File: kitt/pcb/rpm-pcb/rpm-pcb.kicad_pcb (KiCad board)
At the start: 2 copper layers, 0 parts

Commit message: placed rpm leds
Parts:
- added C1: 100nF, Capacitor_THT:C_Rect_L7.0mm_W3.5mm_P5.00mm, F.Cu at (287.7, -26.9)
- added C10: 100nF, Capacitor_THT:C_Rect_L7.0mm_W3.5mm_P5.00mm, F.Cu at (213.9, 50.4)
- added C11: 100nF, Capacitor_THT:C_Rect_L7.0mm_W3.5mm_P5.00mm, F.Cu at (128.4, 45.3)
- added C12: 100nF, Capacitor_THT:C_Rect_L7.0mm_W3.5mm_P5.00mm, F.Cu at (181.5, 48.3)
- added C13: 100nF, Capacitor_THT:C_Rect_L7.0mm_W3.5mm_P5.00mm, F.Cu at (128.4, 50.3)
- added C2: 1uF, Capacitor_THT:C_Rect_L7.0mm_W3.5mm_P5.00mm, F.Cu at (296.2, -31.9)
- added C3: 100nF, Capacitor_THT:C_Rect_L7.0mm_W3.5mm_P5.00mm, F.Cu at (287.7, -31.9)
- added C4: 100nF, Capacitor_THT:C_Rect_L7.0mm_W3.5mm_P5.00mm, F.Cu at (305.8, -42.7)
- added C5: 100nF, Capacitor_THT:C_Rect_L7.0mm_W3.5mm_P5.00mm, F.Cu at (305.8, -47.7)
- added C6: 100nF, Capacitor_THT:C_Rect_L7.0mm_W3.5mm_P5.00mm, F.Cu at (250.7, 14.5)
- added C7: 100nF, Capacitor_THT:C_Rect_L7.0mm_W3.5mm_P5.00mm, F.Cu at (250.7, 9.45)
- added C8: 100nF, Capacitor_THT:C_Rect_L7.0mm_W3.5mm_P5.00mm, F.Cu at (231.0, 33.7)
- added C9: 1uF, Capacitor_THT:C_Rect_L7.0mm_W3.5mm_P5.00mm, F.Cu at (243.2, 21.6)
- added CG1: LED, KITT-Footpads:Flangeless_LED, F.Cu at (67.2, 116.8)
- added CG10: LED, KITT-Footpads:Flangeless_LED, F.Cu at (107.1, 93.7)
- added CG11: LED, KITT-Footpads:Flangeless_LED, F.Cu at (112.0, 92.0)
- added CG12: LED, KITT-Footpads:Flangeless_LED, F.Cu at (116.9, 90.6)
- added CG13: LED, KITT-Footpads:Flangeless_LED, F.Cu at (121.9, 89.4)
- added CG14: LED, KITT-Footpads:Flangeless_LED, F.Cu at (126.9, 88.3)
- added CG15: LED, KITT-Footpads:Flangeless_LED, F.Cu at (132.0, 87.5)
- added CG16: LED, KITT-Footpads:Flangeless_LED, F.Cu at (137.1, 86.9)
- added CG17: LED, KITT-Footpads:Flangeless_LED, F.Cu at (142.2, 86.5)
- added CG18: LED, KITT-Footpads:Flangeless_LED, F.Cu at (147.4, 86.2)
- added CG19: LED, KITT-Footpads:Flangeless_LED, F.Cu at (152.5, 86.2)
- added CG2: LED, KITT-Footpads:Flangeless_LED, F.Cu at (71.2, 113.5)
- added CG20: LED, KITT-Footpads:Flangeless_LED, F.Cu at (157.7, 86.5)
- added CG21: LED, KITT-Footpads:Flangeless_LED, F.Cu at (162.8, 86.9)
- added CG22: LED, KITT-Footpads:Flangeless_LED, F.Cu at (167.9, 87.5)
- added CG23: LED, KITT-Footpads:Flangeless_LED, F.Cu at (173.0, 88.3)
- added CG24: LED, KITT-Footpads:Flangeless_LED, F.Cu at (178.1, 89.4)
- added CG25: LED, KITT-Footpads:Flangeless_LED, F.Cu at (183.1, 90.7)
- added CG26: LED, KITT-Footpads:Flangeless_LED, F.Cu at (188.0, 92.0)
- added CG27: LED, KITT-Footpads:Flangeless_LED, F.Cu at (258.5, 19.9)
- added CG28: LED, KITT-Footpads:Flangeless_LED, F.Cu at (192.9, 93.7)
- added CG29: LED, KITT-Footpads:Flangeless_LED, F.Cu at (197.7, 95.5)
- added CG3: LED, KITT-Footpads:Flangeless_LED, F.Cu at (75.3, 110.4)
- added CG30: LED, KITT-Footpads:Flangeless_LED, F.Cu at (202.5, 97.5)
- added CG4: LED, KITT-Footpads:Flangeless_LED, F.Cu at (79.5, 107.5)
- added CG5: LED, KITT-Footpads:Flangeless_LED, F.Cu at (83.9, 104.8)
- added CG6: LED, KITT-Footpads:Flangeless_LED, F.Cu at (88.3, 102.2)
- added CG7: LED, KITT-Footpads:Flangeless_LED, F.Cu at (92.9, 99.8)
- added CG8: LED, KITT-Footpads:Flangeless_LED, F.Cu at (97.5, 97.5)
- added CG9: LED, KITT-Footpads:Flangeless_LED, F.Cu at (102.3, 95.5)
- added CT_DISP1: LDS-A816RI, KITT-Footpads:LDS-A816RI, F.Cu at (132.2, 104.6)
- added CT_DISP2: LDS-A816RI, KITT-Footpads:LDS-A816RI, F.Cu at (152.5, 104.6)
- added J1: Screw_Terminal_01x02, KITT-Footpads:5mm_Screw_Terminal_01x02, F.Cu at (316.1, -54.4)
- added J2: Screw_Terminal_01x02, KITT-Footpads:5mm_Screw_Terminal_01x02, F.Cu at (182.7, 41.0)
- added KEG_1_CAP_L1: 125807R, KITT-Footpads:LED_12_Segment_2.0mm_24_pin, F.Cu at (125.5, -9.80)
- added KEG_1_CAP_R1: 125807R, KITT-Footpads:LED_12_Segment_2.0mm_24_pin, F.Cu at (117.4, -68.9)
- added KEG_1_T1: STBD01-4R8GA, KITT-Footpads:LED_12_Segment_2.0mm_24_pin, F.Cu at (223.0, -68.9)
- added KEG_2_T1: STBD01-4R8GA, KITT-Footpads:LED_12_Segment_2.0mm_24_pin, F.Cu at (214.9, -68.9)
- added KEG_3_T1: STBD01-4R8GA, KITT-Footpads:LED_12_Segment_2.0mm_24_pin, F.Cu at (206.7, -68.9)
- added KEG_4_T1: STBD01-4R8GA, KITT-Footpads:LED_12_Segment_2.0mm_24_pin, F.Cu at (198.6, -68.9)
- added KEG_5_T1: STBD01-4R8GA, KITT-Footpads:LED_12_Segment_2.0mm_24_pin, F.Cu at (190.5, -68.9)
- added KEG_CAP_2_L1: 125807R, KITT-Footpads:LED_12_Segment_2.0mm_24_pin, F.Cu at (182.4, -68.9)
- added KEG_CAP_2_R1: 125807R, KITT-Footpads:LED_12_Segment_2.0mm_24_pin, F.Cu at (174.3, -68.9)
- added KEG_CAP_3_L1: 125807R, KITT-Footpads:LED_12_Segment_2.0mm_24_pin, F.Cu at (166.1, -68.9)
- added KEG_CAP_3_R1: 125807R, KITT-Footpads:LED_12_Segment_2.0mm_24_pin, F.Cu at (158.0, -68.9)
- added LAGER_1_T_L1: 125807R, KITT-Footpads:LED_12_Segment_2.0mm_24_pin, F.Cu at (149.9, -68.9)
- added LAGER_1_T_R1: STBD01-4R8GA, KITT-Footpads:LED_12_Segment_2.0mm_24_pin, F.Cu at (141.8, -68.9)
- added LAGER_2_T_L1: 125807R, KITT-Footpads:LED_12_Segment_2.0mm_24_pin, F.Cu at (133.7, -68.9)
- added LAGER_2_T_R1: STBD01-4R8GA, KITT-Footpads:LED_12_Segment_2.0mm_24_pin, F.Cu at (125.5, -68.9)
- added LAGER_3_T_L1: 125807R, KITT-Footpads:LED_12_Segment_2.0mm_24_pin, F.Cu at (117.4, -9.80)
- added LAGER_3_T_R1: STBD01-4R8GA, KITT-Footpads:LED_12_Segment_2.0mm_24_pin, F.Cu at (133.7, -9.80)
- added LINE_T1: STBD01-4R8GA, KITT-Footpads:LED_12_Segment_2.0mm_24_pin, F.Cu at (231.1, -68.9)
- added LVL1: LVL_5V_3V3, KITT-Footpads:LVL_5V_3V3, F.Cu at (227.0, 23.0)
- added LVL2: LVL_5V_3V3, KITT-Footpads:LVL_5V_3V3, F.Cu at (283.7, -36.1)
- added LVL3: LVL_5V_3V3, KITT-Footpads:LVL_5V_3V3, F.Cu at (314.7, -73.3)
- added MH1: MountingHole, MountingHole:MountingHole_3.2mm_M3, F.Cu at (62.0, 71.5)
- added MH2: MountingHole, MountingHole:MountingHole_3.2mm_M3, F.Cu at (202.0, 71.5)
- added MH3: MountingHole, MountingHole:MountingHole_3.2mm_M3, F.Cu at (248.0, 71.5)
- added MH4: MountingHole, MountingHole:MountingHole_3.2mm_M3, F.Cu at (344.0, 71.5)
- added MH5: MountingHole, MountingHole:MountingHole_3.2mm_M3, F.Cu at (62.0, 195.5)
- added MH6: MountingHole, MountingHole:MountingHole_3.2mm_M3, F.Cu at (202.0, 195.5)
- added MH7: MountingHole, MountingHole:MountingHole_3.2mm_M3, F.Cu at (248.0, 195.5)
- added MH8: MountingHole, MountingHole:MountingHole_3.2mm_M3, F.Cu at (344.0, 195.5)
- added NT1: Net-Tie_3_Tee, NetTie:NetTie-3_THT_Pad0.3mm, F.Cu at (119.0, 51.9)
- added NT10: Net-Tie_3_Tee, NetTie:NetTie-3_THT_Pad0.3mm, F.Cu at (194.8, 50.8)
- added NT11: Net-Tie_3_Tee, NetTie:NetTie-3_THT_Pad0.3mm, F.Cu at (287.0, -37.4)
- added NT12: Net-Tie_3_Tee, NetTie:NetTie-3_THT_Pad0.3mm, F.Cu at (199.3, 50.8)
- added NT13: Net-Tie_3_Tee, NetTie:NetTie-3_THT_Pad0.3mm, F.Cu at (114.4, 51.9)
- added NT2: Net-Tie_3_Tee, NetTie:NetTie-3_THT_Pad0.3mm, F.Cu at (224.6, -3.36)
- added NT3: Net-Tie_3_Tee, NetTie:NetTie-3_THT_Pad0.3mm, F.Cu at (167.5, 50.3)
- added NT4: Net-Tie_3_Tee, NetTie:NetTie-3_THT_Pad0.3mm, F.Cu at (172.0, 50.3)
- added NT5: Net-Tie_3_Tee, NetTie:NetTie-3_THT_Pad0.3mm, F.Cu at (229.1, -3.36)
- added NT6: Net-Tie_3_Tee, NetTie:NetTie-3_THT_Pad0.3mm, F.Cu at (176.6, 51.9)
- added NT7: Net-Tie_3_Tee, NetTie:NetTie-3_THT_Pad0.3mm, F.Cu at (181.1, 51.9)
- added NT8: Net-Tie_3_Tee, NetTie:NetTie-3_THT_Pad0.3mm, F.Cu at (185.7, 51.9)
- added NT9: Net-Tie_3_Tee, NetTie:NetTie-3_THT_Pad0.3mm, F.Cu at (190.2, 50.8)
- added PEG1: MountingHole, MountingHole:MountingHole_5.3mm_M5, F.Cu at (45.0, 72.0)
- added PEG2: MountingHole, MountingHole:MountingHole_5.3mm_M5, F.Cu at (220.0, 72.0)
- added PEG3: MountingHole, MountingHole:MountingHole_5.3mm_M5, F.Cu at (445.0, 72.0)
- added PEG4: MountingHole, MountingHole:MountingHole_5.3mm_M5, F.Cu at (45.0, 197.0)
- added PEG5: MountingHole, MountingHole:MountingHole_5.3mm_M5, F.Cu at (220.0, 197.0)
- added PEG6: MountingHole, MountingHole:MountingHole_5.3mm_M5, F.Cu at (445.0, 197.0)
- added PWR1: OKI-78SR-5_1.5-W36H-C, Converter_DCDC:Converter_DCDC_muRata_OKI-78SR_Horizontal, F.Cu at (260.3, -36.3)
- added Q1: NDP6020P, Package_TO_SOT_THT:TO-220-3_Vertical, F.Cu at (226.7, -6.47)
- added Q2: NDP6020P, Package_TO_SOT_THT:TO-220-3_Vertical, F.Cu at (226.7, -12.4)
- added Q3: NDP6020P, Package_TO_SOT_THT:TO-220-3_Vertical, F.Cu at (320.1, -63.5)
- added Q4: NDP6020P, Package_TO_SOT_THT:TO-220-3_Vertical, F.Cu at (333.4, -71.6)
- added Q5: NDP6020P, Package_TO_SOT_THT:TO-220-3_Vertical, F.Cu at (273.4, -13.2)
- added Q6: NDP6020P, Package_TO_SOT_THT:TO-220-3_Vertical, F.Cu at (215.4, 45.9)
- added R1: 120R, Resistor_THT:R_Axial_DIN0207_L6.3mm_D2.5mm_P10.16mm_Horizontal, F.Cu at (301.3, -52.3)
- added R10: 120R, Resistor_THT:R_Axial_DIN0207_L6.3mm_D2.5mm_P10.16mm_Horizontal, F.Cu at (280.1, -44.6)
- added R11: 120R, Resistor_THT:R_Axial_DIN0207_L6.3mm_D2.5mm_P10.16mm_Horizontal, F.Cu at (168.0, 47.2)
- added R12: 120R, Resistor_THT:R_Axial_DIN0207_L6.3mm_D2.5mm_P10.16mm_Horizontal, F.Cu at (168.0, 43.2)
- added R13: 10K, Resistor_THT:R_Axial_DIN0207_L6.3mm_D2.5mm_P10.16mm_Horizontal, F.Cu at (168.0, 39.1)
- added R14: 2.2K, Resistor_THT:R_Axial_DIN0207_L6.3mm_D2.5mm_P10.16mm_Horizontal, F.Cu at (114.9, 48.8)
- added R15: 2.2K, Resistor_THT:R_Axial_DIN0207_L6.3mm_D2.5mm_P10.16mm_Horizontal, F.Cu at (114.9, 44.8)
- added R16: 2.2K, Resistor_THT:R_Axial_DIN0207_L6.3mm_D2.5mm_P10.16mm_Horizontal, F.Cu at (225.1, 0.85)
- added R17: 2.2K, Resistor_THT:R_Axial_DIN0207_L6.3mm_D2.5mm_P10.16mm_Horizontal, F.Cu at (225.1, 4.90)
- added R18: 2.2K, Resistor_THT:R_Axial_DIN0207_L6.3mm_D2.5mm_P10.16mm_Horizontal, F.Cu at (225.1, 8.95)
- added R19: 10K, Resistor_THT:R_Axial_DIN0207_L6.3mm_D2.5mm_P10.16mm_Horizontal, F.Cu at (238.4, 0.85)
- added R2: 120R, Resistor_THT:R_Axial_DIN0207_L6.3mm_D2.5mm_P10.16mm_Horizontal, F.Cu at (258.4, -14.2)
- added R20: 2.2K, Resistor_THT:R_Axial_DIN0207_L6.3mm_D2.5mm_P10.16mm_Horizontal, F.Cu at (318.4, -69.4)
- added R21: 2.2K, Resistor_THT:R_Axial_DIN0207_L6.3mm_D2.5mm_P10.16mm_Horizontal, F.Cu at (238.4, 4.90)
- added R22: 2.2K, Resistor_THT:R_Axial_DIN0207_L6.3mm_D2.5mm_P10.16mm_Horizontal, F.Cu at (225.1, 13.0)
- added R23: 2.2K, Resistor_THT:R_Axial_DIN0207_L6.3mm_D2.5mm_P10.16mm_Horizontal, F.Cu at (225.1, 17.0)
- added R3: 120R, Resistor_THT:R_Axial_DIN0207_L6.3mm_D2.5mm_P10.16mm_Horizontal, F.Cu at (271.7, -19.2)
- added R4: 120R, Resistor_THT:R_Axial_DIN0207_L6.3mm_D2.5mm_P10.16mm_Horizontal, F.Cu at (213.7, 39.9)
- added R5: 120R, Resistor_THT:R_Axial_DIN0207_L6.3mm_D2.5mm_P10.16mm_Horizontal, F.Cu at (258.4, -18.3)
- added R6: 120R, Resistor_THT:R_Axial_DIN0207_L6.3mm_D2.5mm_P10.16mm_Horizontal, F.Cu at (301.3, -56.3)
- added R7: 120R, Resistor_THT:R_Axial_DIN0207_L6.3mm_D2.5mm_P10.16mm_Horizontal, F.Cu at (318.4, -73.5)
- added R8: 120R, Resistor_THT:R_Axial_DIN0207_L6.3mm_D2.5mm_P10.16mm_Horizontal, F.Cu at (258.4, -10.2)
- added R9: 120R, Resistor_THT:R_Axial_DIN0207_L6.3mm_D2.5mm_P10.16mm_Horizontal, F.Cu at (280.1, -40.5)
- added RPM1: KB2855SGD, KITT-Footpads:KB2855SGD_Light_Square, F.Cu at (231.0, 43.4)
- added RPM2: KB2855SGD, KITT-Footpads:KB2855SGD_Light_Square, F.Cu at (335.7, -64.0)
- added RPM3: KB2855SGD, KITT-Footpads:KB2855SGD_Light_Square, F.Cu at (275.7, -5.67)
- added THRU1: MountingHole, MountingHole:MountingHole_6.4mm_M6, F.Cu at (46.1, 26.1)
- added THRU2: MountingHole, MountingHole:MountingHole_6.4mm_M6, F.Cu at (46.3, 7.82)
- added TTGO1: TTGO_ESP32_TDISPLAY_V1.1, KITT-Footpads:TTGO_ESP32_TDisplay_v1.1, F.Cu at (140.8, 36.3)
- added TTGO2: TTGO_ESP32_TDISPLAY_V1.1, KITT-Footpads:TTGO_ESP32_TDisplay_v1.1, F.Cu at (140.8, 9.62)
- added U1: TLC5940NT, Package_DIP:DIP-28_W7.62mm, F.Cu at (203.4, -14.3)
- added U2: TLC5940NT, Package_DIP:DIP-28_W7.62mm, F.Cu at (247.6, -73.4)
- added U3: TLC5940NT, Package_DIP:DIP-28_W7.62mm, F.Cu at (192.6, -14.3)
- added U4: TLC5940NT, Package_DIP:DIP-28_W7.62mm, F.Cu at (236.8, -73.4)
- added U5: TLC5940NT, Package_DIP:DIP-28_W7.62mm, F.Cu at (247.6, -36.3)
- added U6: TLC5940NT, Package_DIP:DIP-28_W7.62mm, F.Cu at (236.8, -36.3)
- added U7: TLC5940NT, Package_DIP:DIP-28_W7.62mm, F.Cu at (214.3, -14.3)
- added U8: TLC5940NT, Package_DIP:DIP-28_W7.62mm, F.Cu at (269.3, -73.4)
- added U9: TLC5940NT, Package_DIP:DIP-28_W7.62mm, F.Cu at (258.5, -73.4)
- added YD1: LED, KITT-Footpads:Flangeless_LED, F.Cu at (259.2, 32.1)
- added YD10: LED, KITT-Footpads:Flangeless_LED, F.Cu at (303.1, -12.1)
- added YD11: LED, KITT-Footpads:Flangeless_LED, F.Cu at (330.6, -33.8)
- added YD12: LED, KITT-Footpads:Flangeless_LED, F.Cu at (309.3, -12.1)
- added YD13: LED, KITT-Footpads:Flangeless_LED, F.Cu at (303.1, -5.94)
- added YD14: LED, KITT-Footpads:Flangeless_LED, F.Cu at (325.1, -27.7)
- added YD15: LED, KITT-Footpads:Flangeless_LED, F.Cu at (319.0, -21.5)
- added YD16: LED, KITT-Footpads:Flangeless_LED, F.Cu at (276.9, 20.0)
- added YD17: LED, KITT-Footpads:Flangeless_LED, F.Cu at (270.8, 26.1)
- added YD18: LED, KITT-Footpads:Flangeless_LED, F.Cu at (259.2, 38.2)
- added YD19: LED, KITT-Footpads:Flangeless_LED, F.Cu at (251.8, 44.4)
- added YD2: LED, KITT-Footpads:Flangeless_LED, F.Cu at (253.1, 38.2)
- added YD20: LED, KITT-Footpads:Flangeless_LED, F.Cu at (336.7, -38.3)
- added YD21: LED, KITT-Footpads:Flangeless_LED, F.Cu at (285.0, 13.9)
- added YD25: LED, KITT-Footpads:Flangeless_LED, F.Cu at (293.0, 6.89)
- added YD26: LED, KITT-Footpads:Flangeless_LED, F.Cu at (299.1, 0.18)
- added YD27: LED, KITT-Footpads:Flangeless_LED, F.Cu at (297.0, -7.40)
- added YD3: LED, KITT-Footpads:Flangeless_LED, F.Cu at (337.6, -44.4)
- added YD31: LED, KITT-Footpads:Flangeless_LED, F.Cu at (284.3, -5.35)
- added YD32: LED, KITT-Footpads:Flangeless_LED, F.Cu at (290.9, -11.5)
- added YD33: LED, KITT-Footpads:Flangeless_LED, F.Cu at (321.7, -39.9)
- added YD37: LED, KITT-Footpads:Flangeless_LED, F.Cu at (284.8, -11.5)
- added YD38: LED, KITT-Footpads:Flangeless_LED, F.Cu at (294.5, -19.6)
- added YD39: LED, KITT-Footpads:Flangeless_LED, F.Cu at (306.1, -30.4)
- added YD4: LED, KITT-Footpads:Flangeless_LED, F.Cu at (293.0, 0.77)
- added YD43: LED, KITT-Footpads:Flangeless_LED, F.Cu at (260.6, 13.8)
- added YD44: LED, KITT-Footpads:Flangeless_LED, F.Cu at (268.5, 5.81)
- added YD45: LED, KITT-Footpads:Flangeless_LED, F.Cu at (240.9, 33.9)
- added YD49: LED, KITT-Footpads:Flangeless_LED, F.Cu at (252.4, 25.9)
- added YD5: LED, KITT-Footpads:Flangeless_LED, F.Cu at (286.9, 6.89)
- added YD50: LED, KITT-Footpads:Flangeless_LED, F.Cu at (335.2, -56.7)
- added YD51: LED, KITT-Footpads:Flangeless_LED, F.Cu at (253.2, 0.61)
- added YD6: LED, KITT-Footpads:Flangeless_LED, F.Cu at (278.9, 13.9)
- added YD7: LED, KITT-Footpads:Flangeless_LED, F.Cu at (270.8, 20.0)
- added YD8: LED, KITT-Footpads:Flangeless_LED, F.Cu at (312.8, -18.2)
- added YD9: LED, KITT-Footpads:Flangeless_LED, F.Cu at (319.0, -27.7)
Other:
- board outline added: 430 x 139 mm

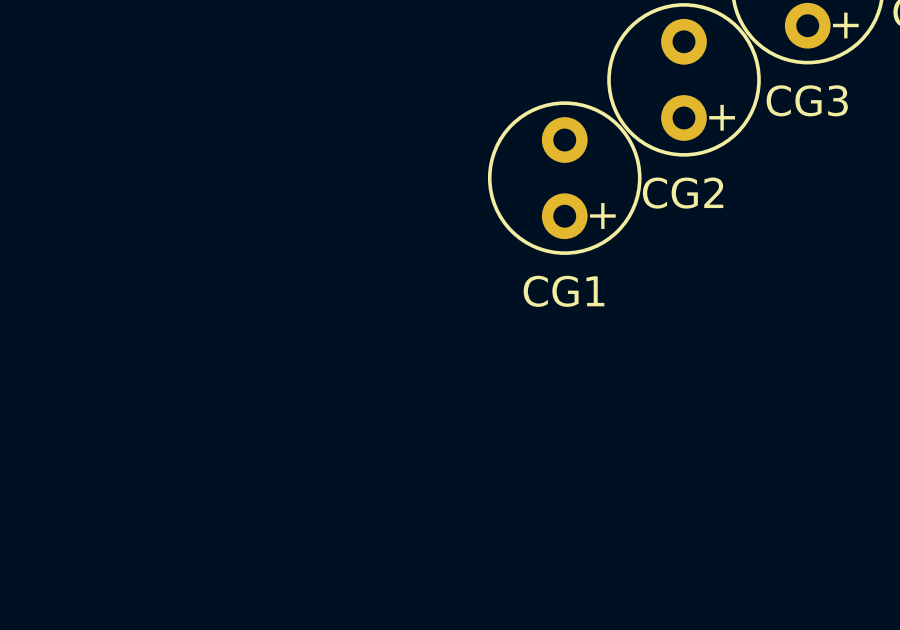
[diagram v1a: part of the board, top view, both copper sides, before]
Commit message: added extra cg led
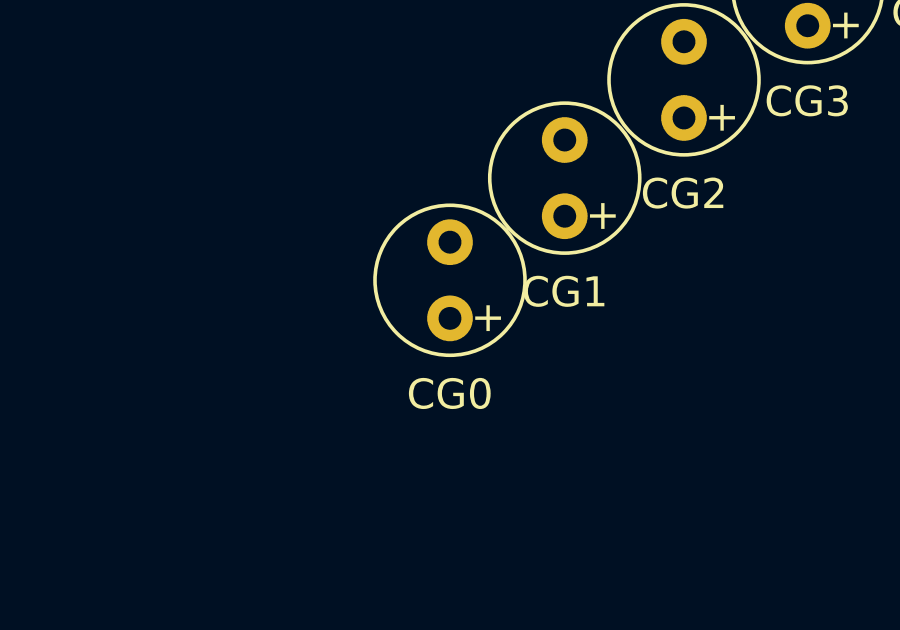
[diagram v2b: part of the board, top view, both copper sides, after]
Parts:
- added CG0: LED, KITT-Footpads:Flangeless_LED, F.Cu at (63.4, 120.2)
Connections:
- U2 pad 28: Net-(U2-Pad28) -> /CG_D0

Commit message: reworked rpm leds
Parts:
- moved CT_DISP1 100.0 mm to (232.2, 104.6)
- moved CT_DISP2 100.0 mm to (252.5, 104.6)
- moved MH1 100.0 mm to (162.0, 71.5)
- moved MH2 100.0 mm to (302.0, 71.5)
- moved MH3 100.0 mm to (348.0, 71.5)
- moved MH5 100.0 mm to (162.0, 195.5)
- moved MH6 100.0 mm to (302.0, 195.5)
- moved MH7 100.0 mm to (348.0, 195.5)
- moved PEG1 100.0 mm to (145.0, 72.0)
- moved PEG2 100.0 mm to (320.0, 72.0)
- moved PEG4 100.0 mm to (145.0, 197.0)
- moved PEG5 100.0 mm to (320.0, 197.0)
- moved CG0 98.3 mm to (161.6, 122.6)
- moved CG1 98.2 mm to (165.4, 119.0)
- moved CG2 98.2 mm to (169.3, 115.7)
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
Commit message: moved back from print position
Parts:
- moved CG23 100.0 mm to (171.0, 89.3)
- moved CG24 100.0 mm to (176.0, 90.5)
- moved CG25 100.0 mm to (181.0, 91.8)
- moved CG11 100.0 mm to (110.0, 93.2)
- moved CG14 100.0 mm to (124.9, 89.4)
- moved CG15 100.0 mm to (130.0, 88.5)
- moved CG16 100.0 mm to (135.1, 87.9)
- moved CG17 100.0 mm to (140.2, 87.5)
- moved CG18 100.0 mm to (145.4, 87.2)
- moved CG19 100.0 mm to (150.5, 87.2)
- moved CG2 100.0 mm to (69.3, 115.7)
- moved CG20 100.0 mm to (155.7, 87.5)
- moved CG22 100.0 mm to (165.9, 88.5)
- moved CG26 100.0 mm to (186.0, 93.2)
- moved CG28 100.0 mm to (190.9, 95.0)
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
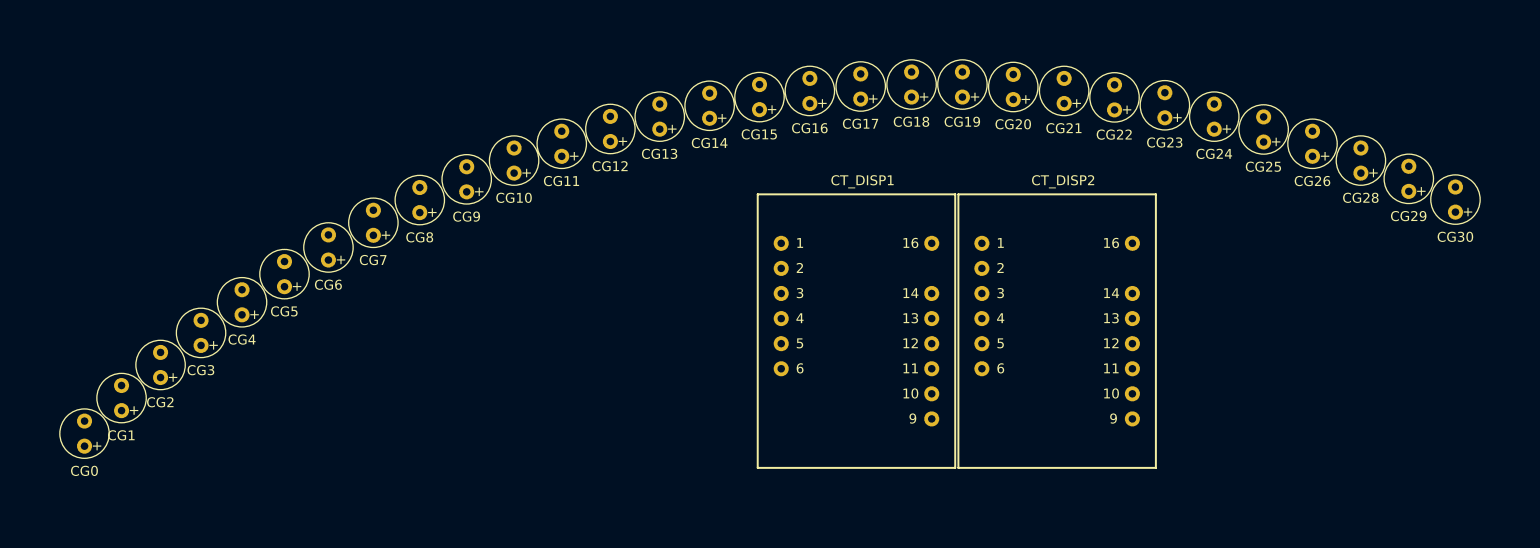
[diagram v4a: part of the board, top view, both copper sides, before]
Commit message: reposition based on printout
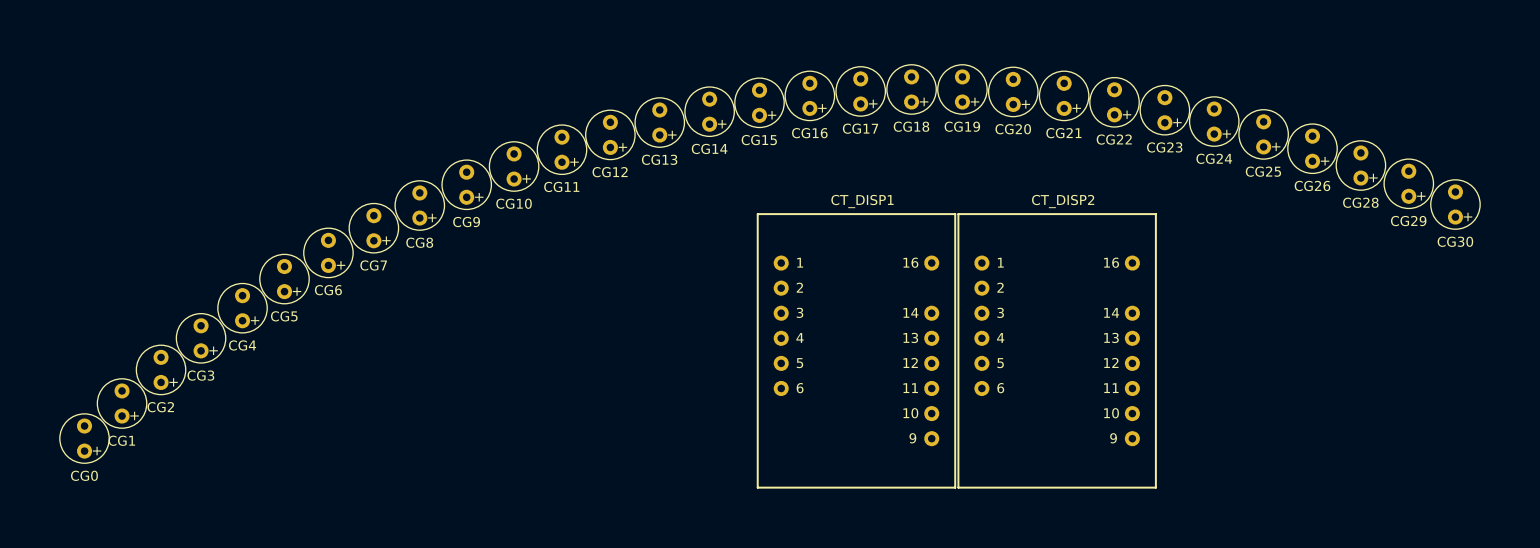
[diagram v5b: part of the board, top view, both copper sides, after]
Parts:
- moved CT_DISP1 2.00 mm to (132.2, 106.6)
- moved CT_DISP2 2.00 mm to (152.5, 106.6)
- moved CG4 0.60 mm to (77.6, 109.9)
- moved CG11 0.60 mm to (110.0, 93.8)
- moved CG10 0.60 mm to (105.1, 95.5)
- moved CG12 0.60 mm to (114.9, 92.3)
- moved CG13 0.60 mm to (119.9, 91.1)
- moved CG14 0.60 mm to (124.9, 90.0)
- moved CG15 0.57 mm to (130.0, 89.1)
- moved CG1 0.55 mm to (65.4, 119.5)
- moved CG7 0.55 mm to (90.9, 101.8)
- moved CG9 0.55 mm to (100.3, 97.4)
- moved CG3 0.55 mm to (73.4, 113.0)
- moved CG6 0.55 mm to (86.3, 104.3)
- moved CG8 0.55 mm to (95.6, 99.5)
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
